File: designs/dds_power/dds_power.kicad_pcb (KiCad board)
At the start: 4 copper layers, 64.8 x 52.7 mm, 25 parts, among them K1 3.3_1.8, K2 3.3_1.8, K3 3.3_1.8, K4 3.3_1.8, K5 3.3_1.8, K6 3.3_1.8, P1 CONN_3, P2 12V, P3 12V, P4 12V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

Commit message: [designs/dds_power] update to kicad 4.0, add missing mount hole
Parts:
- added REF**: MountingHole_3.2mm_M3_Pad, Mounting_Holes:MountingHole_3.2mm_M3_Pad, F.Cu at (134.6, 135.3)
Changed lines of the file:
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@@
-(kicad_pcb (version 4) (host pcbnew "(2015-05-27 BZR 5686)-product")
+(kicad_pcb (version 4) (host pcbnew 4.0.4-stable)
   (general
     (links 51)
     (no_connects 0)
-    (area 128.854999 93.929999 197.894762 146.735001)
+    (area 128.854999 93.929999 197.29 146.735001)
     (thickness 1.6)
     (drawings 15)
     (tracks 393)
     (zones 0)
-    (modules 25)
+    (modules 26)
     (nets 13)
   )
@@
       (net 6 "Net-(C5-Pad2)"))
   )
+  (module Mounting_Holes:MountingHole_3.2mm_M3_Pad (layer F.Cu)
+    (at 134.62 135.255)
+    (descr "Mounting Hole 3.2mm, M3")
+    (tags "mounting hole 3.2mm m3")
+    (fp_text reference REF** (at 0 -4.2) (layer F.SilkS)
+      (effects (font (size 1 1) (thickness 0.15)))
+    )
+    (fp_text value MountingHole_3.2mm_M3_Pad (at 0 4.2) (layer F.Fab)
+      (effects (font (size 1 1) (thickness 0.15)))
+    )
+    (fp_circle (center 0 0) (end 3.2 0) (layer Cmts.User) (width 0.15))
+    (fp_circle (center 0 0) (end 3.45 0) (layer F.CrtYd) (width 0.05))
+    (pad 1 thru_hole circle (at 0 0) (size 6.4 6.4) (drill 3.2) (layers *.Cu *.Mask F.SilkS))
+  )
   (gr_line (start 128.905 146.685) (end 128.905 93.98) (angle 90) (layer Edge.Cuts) (width 0.1))

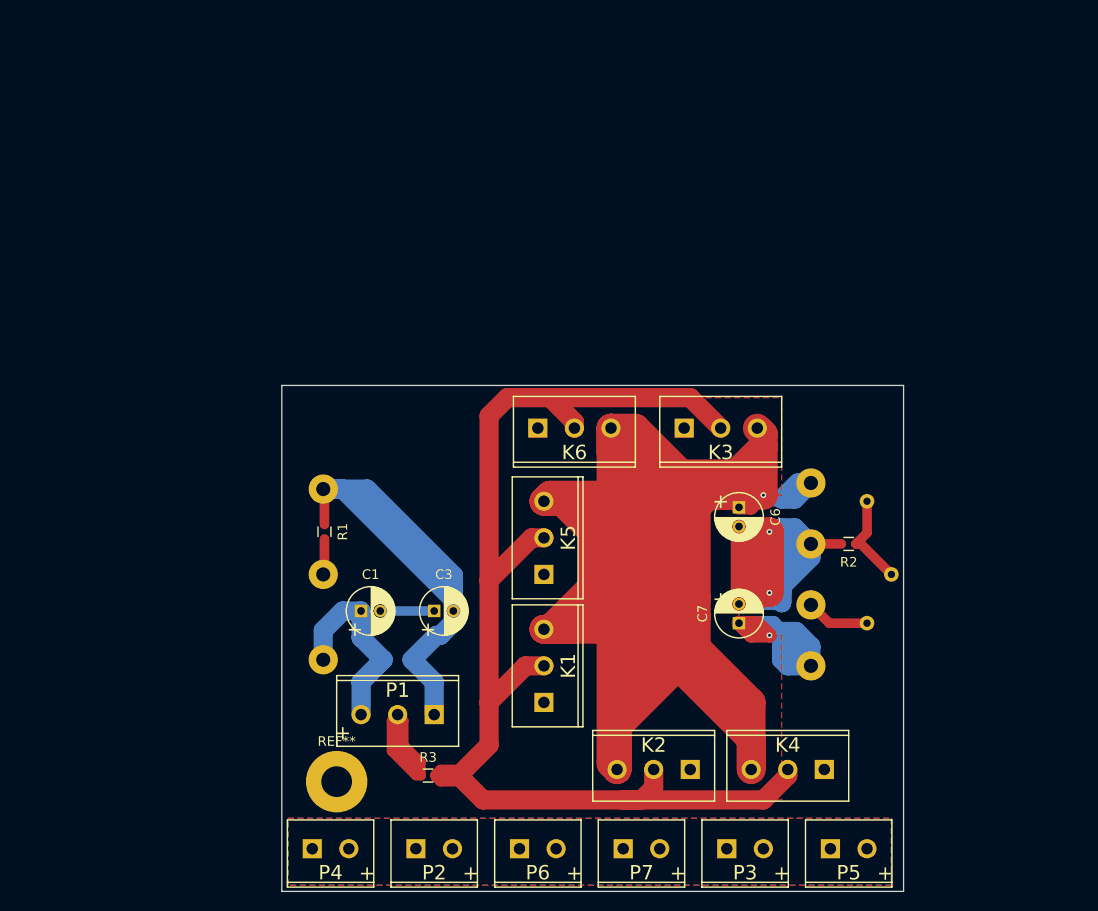
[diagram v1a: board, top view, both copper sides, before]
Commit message: [designs/dds_power] update for new power requirements
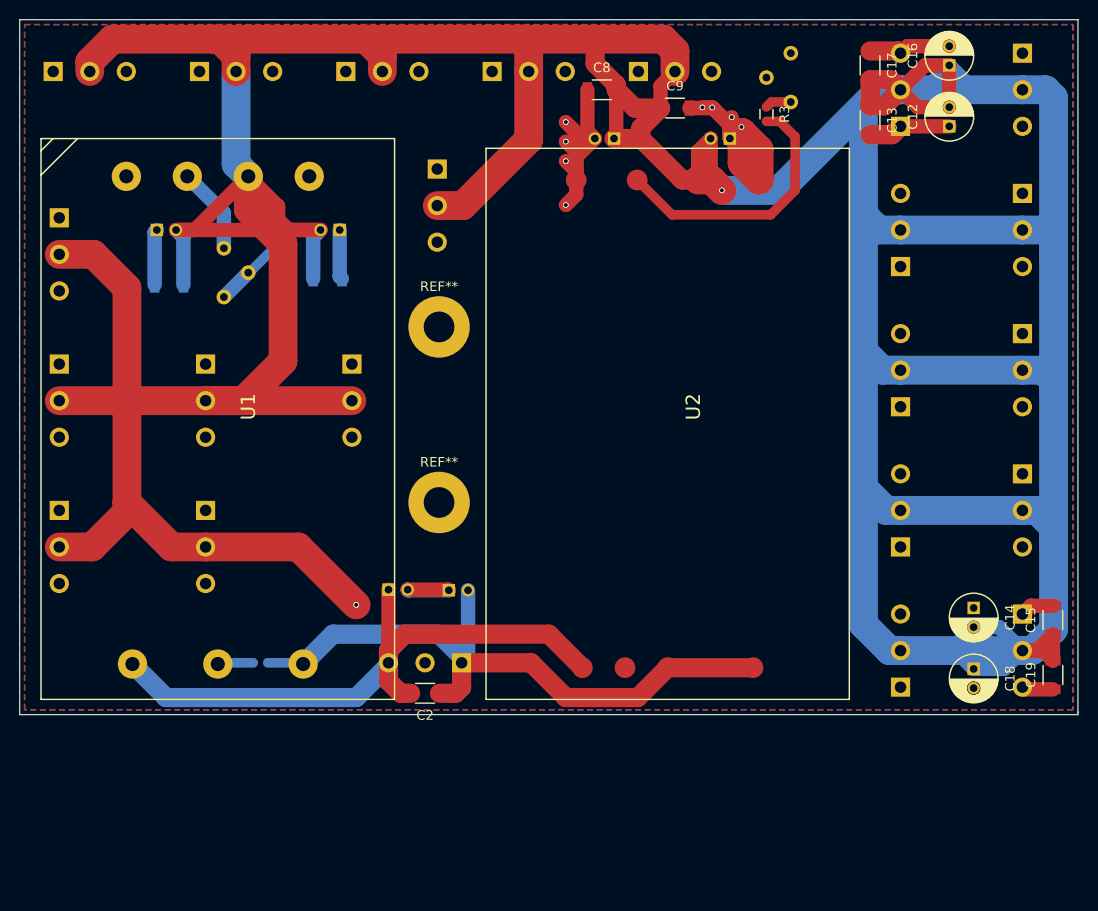
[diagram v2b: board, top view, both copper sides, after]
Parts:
- removed P2, P3, P4, P5, P6, P7: 12V, cmr_link:2-pins_150mil
- removed the REF** at (134.6, 135.3)
- added C10: CP, Capacitors_ThroughHole:C_Radial_D5_L11_P2, B.Cu at (163.5, 68.3)
- added C11: CP, Capacitors_ThroughHole:C_Radial_D5_L11_P2, B.Cu at (175.6, 68.3)
- added C12: CP, Capacitors_ThroughHole:C_Radial_D5_L11_P2, F.Cu at (198.4, 67.0)
- added C13: C, Capacitors_SMD:C_1206, F.Cu at (190.2, 66.4)
- added C14: CP, Capacitors_ThroughHole:C_Radial_D5_L11_P2, F.Cu at (201.0, 117.2)
- added C15: C, Capacitors_SMD:C_1206, F.Cu at (209.2, 118.4)
- added C16: CP, Capacitors_ThroughHole:C_Radial_D5_L11_P2, F.Cu at (198.4, 60.6)
- added C17: C, Capacitors_SMD:C_1206, F.Cu at (190.2, 60.6)
- added C18: CP, Capacitors_ThroughHole:C_Radial_D5_L11_P2, F.Cu at (201.0, 123.5)
- added C19: C, Capacitors_SMD:C_1206, F.Cu at (209.2, 124.1)
- added C8: C, Capacitors_SMD:C_1206, F.Cu at (162.2, 63.2)
- added C9: C, Capacitors_SMD:C_1206, F.Cu at (169.9, 65.1)
- added K10: +-12, cmr_link:3-pins_150mil, B.Cu at (139.4, 61.3)
- added K11: +-12, cmr_link:3-pins_150mil, B.Cu at (124.1, 61.3)
- added K12: +-12, cmr_link:3-pins_150mil, B.Cu at (108.9, 61.3)
- added K13: +-5, cmr_link:3-pins_150mil, B.Cu at (193.4, 121.6)
- added K14: +-5, cmr_link:3-pins_150mil, B.Cu at (206.1, 107.0)
- added K15: +-5, cmr_link:3-pins_150mil, B.Cu at (193.4, 107.0)
- added K16: +-5, cmr_link:3-pins_150mil, B.Cu at (206.1, 63.2)
- added K17: +-5, cmr_link:3-pins_150mil, B.Cu at (193.4, 77.8)
- added K18: +-5, cmr_link:3-pins_150mil, B.Cu at (206.1, 77.8)
- added K19: +-5, cmr_link:3-pins_150mil, B.Cu at (193.4, 63.2)
- added K20: +-5, cmr_link:3-pins_150mil, B.Cu at (206.1, 92.4)
- added K21: +-5, cmr_link:3-pins_150mil, B.Cu at (193.4, 92.4)
- added K22: +-5, cmr_link:3-pins_150mil, B.Cu at (206.1, 121.6)
- added K7: +-12, cmr_link:3-pins_150mil, B.Cu at (154.6, 61.3)
- added K8: +-12, cmr_link:3-pins_150mil, B.Cu at (169.9, 61.3)
- added K9: +-12, cmr_link:3-pins_150mil, B.Cu at (145.1, 75.2)
- added REF**: MountingHole_3.2mm_M3_Pad, Mounting_Holes:MountingHole_3.2mm_M3_Pad, F.Cu at (145.3, 87.9)
- added REF**: MountingHole_3.2mm_M3_Pad, Mounting_Holes:MountingHole_3.2mm_M3_Pad, F.Cu at (145.3, 106.2)
- added RV2: POT, Potentiometers:Potentiometer_Bourns_3296Y_3-8Zoll_Angular_ScrewUp, B.Cu at (181.9, 59.4)
- added U2: PTB48510BAS, ptb48510bas:ptb48510bas, F.Cu at (150.2, 126.7)
- C1, C3, C6, C7, K1, K2, K3, K4, K5, K6, P1, R1, R2: moved to B.Cu
- C2, U1: moved to F.Cu
- RV1: footprint Potentiometers:Potentiometer_Bourns_3005_Angular_ScrewFront -> Potentiometers:Potentiometer_Bourns_3296Y_3-8Zoll_Angular_ScrewUp
- moved R3 77.4 mm to (179.4, 65.7), turned to 270 degrees
- moved C7 73.2 mm to (115.9, 77.8), turned to 0 degrees
- moved C5 72.6 mm to (117.2, 83.5), turned to 180 degrees
- moved K4 71.8 mm to (121.0, 95.6), turned to 270 degrees
- moved RV1 70.3 mm to (122.9, 84.8), turned to 180 degrees
- moved R2 67.5 mm to (128.6, 78.4), turned to 90 degrees
- moved K2 66.1 mm to (105.7, 110.8), turned to 270 degrees
- moved K5 58.5 mm to (105.7, 80.3), turned to 270 degrees
- moved K1 57.5 mm to (105.7, 95.6), turned to 270 degrees
- moved K3 55.1 mm to (121.0, 110.8), turned to 270 degrees
- moved C4 53.3 mm to (133.7, 82.9), turned to 180 degrees
- moved C6 50.6 mm to (134.9, 77.8), turned to 180 degrees
- moved U1 26.3 mm to (103.8, 126.7), turned to 90 degrees
- moved K6 23.4 mm to (136.2, 95.6), turned to 270 degrees
- moved R1 15.2 mm to (126.7, 122.9), turned to 180 degrees
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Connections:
- C4 pad 2: Net-(C4-Pad2) -> GND
- C5 pad 1: Net-(C4-Pad2) -> GND
- C6 pad 2: Net-(C4-Pad2) -> GND
- C7 pad 2: Net-(C4-Pad2) -> GND
- K1 pad 2: Net-(C4-Pad2) -> GND
- K2 pad 2: Net-(C4-Pad2) -> GND
- K3 pad 2: Net-(C4-Pad2) -> GND
- K4 pad 2: Net-(C4-Pad2) -> GND
- K5 pad 2: Net-(C4-Pad2) -> GND
- K6 pad 2: Net-(C4-Pad2) -> GND
- R2 pad 2: Net-(C4-Pad2) -> GND
- R3 pad 1: GND -> Net-(R3-Pad1)
- R3 pad 2: Net-(C4-Pad2) -> Net-(R3-Pad2)
- U1 pad 5: Net-(C4-Pad2) -> GND
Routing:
- net GND: track 22.9 -> 712.6 mm, vias 0 -> 2
- net Net-(C4-Pad2): track 573.6 -> 0.00 mm, vias 2 -> 0
- net Net-(C5-Pad2): track 389.2 -> 158.1 mm, vias 1 -> 0
- net Net-(C4-Pad1): track 394.4 -> 171.5 mm, vias 1 -> 0
- net Net-(C10-Pad2): track 0.00 -> 181.4 mm, vias 0 -> 4
- net Net-(C11-Pad1): track 0.00 -> 146.3 mm, vias 0 -> 4
- net Net-(C18-Pad2): track 0.00 -> 100.7 mm
- net Net-(C12-Pad1): track 0.00 -> 89.4 mm
- net Net-(C16-Pad2): track 0.00 -> 88.9 mm
- net Net-(C14-Pad1): track 0.00 -> 84.4 mm
- net Net-(C1-Pad1): track 20.5 -> 65.7 mm
- net Net-(R3-Pad2): track 0.00 -> 28.2 mm
- net Net-(C2-Pad1): track 57.1 -> 69.2 mm
- net Net-(C1-Pad2): track 5.62 -> 8.72 mm
- net Net-(R3-Pad1): track 0.00 -> 2.76 mm
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- added copper zone on B.Cu, net GND
- added copper zone on F.Cu, net GND
- added copper zone on In1.Cu, net GND
- added copper zone on In2.Cu, net GND
- added copper zone on In1.Cu, net Net-(C10-Pad2)
- added copper zone on In2.Cu, net Net-(C11-Pad1)
- added copper zone on In2.Cu, net Net-(C12-Pad1)
- added copper zone on In1.Cu, net Net-(C14-Pad1)
- added copper zone on In1.Cu, net Net-(C16-Pad2)
- added copper zone on In2.Cu, net Net-(C18-Pad2)
- added copper zone on In2.Cu, net Net-(C4-Pad1)
- added copper zone on In1.Cu, net Net-(C5-Pad2)
- removed copper zone on F.Cu, net Net-(C4-Pad1)
- removed copper zone on In1.Cu, net Net-(C4-Pad2)
- removed copper zone on In2.Cu, net Net-(C5-Pad2)
- removed copper zone on F.Cu, net Net-(P2-Pad1)
- removed copper zone on In2.Cu, net Net-(P2-Pad1)
- removed copper zone on B.Cu, net Net-(P2-Pad2)
- removed copper zone on In1.Cu, net Net-(P2-Pad2)
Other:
- board size 64.8 x 52.7 mm -> 110.2 x 72.4 mm
- board text removed: "+"
